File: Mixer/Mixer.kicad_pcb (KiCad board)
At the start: 2 copper layers, 38.7 x 99.7 mm, 39 parts, among them J1 EURO_PWR_2x5, J2 INPUT_1, J3 INPUT_2, J4 INPUT_3, J5 INPUT_4, J6 OUTPUT, U1 TL082

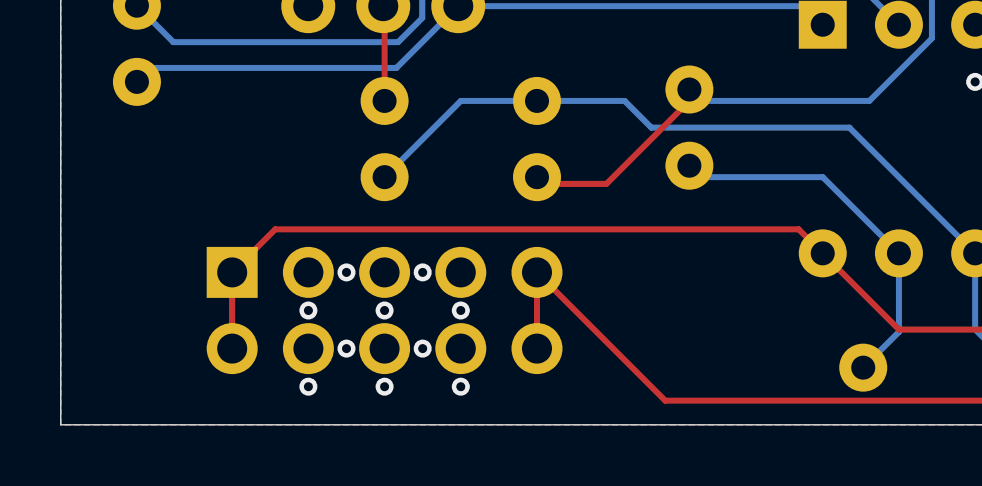
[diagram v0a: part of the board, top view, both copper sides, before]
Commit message: Fix footprint for europower connector, add clearance for shrouded connector
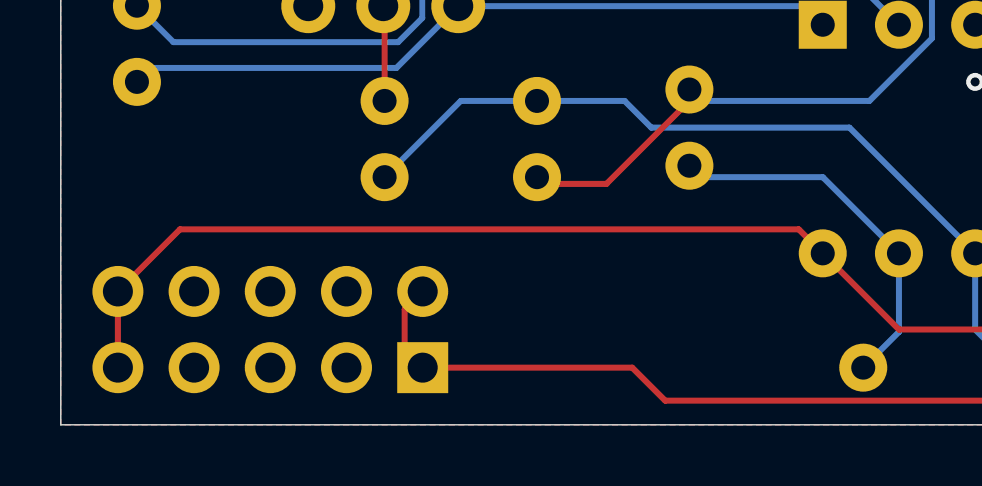
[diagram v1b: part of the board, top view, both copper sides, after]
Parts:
- J1: value EURO_PWR_2x5 -> Europower
- moved J1 7.10 mm to (115.6, 132.7), turned to 90 degrees
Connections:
- J1 pad 1: +12V -> -12V
- J1 pad 10: -12V -> +12V
- J1 pad 2: +12V -> -12V
- J1 pad 9: -12V -> +12V
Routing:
- net +12V: track 35.0 -> 39.1 mm
- net -12V: track 43.1 -> 46.2 mm
- net GND: vias 79 -> 69
